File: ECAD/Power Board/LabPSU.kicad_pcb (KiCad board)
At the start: 2 copper layers, 82 parts, among them J1 CTRL, J2 DC-IN, J3 UPDI, J4 +, J5 -, Q1 Si7148DP, Q2 Si7148DP, U1 LM1117-3.3, U2 LM2594HVN-5.0, U3 LM5118MH, U4 TXB0104D, U5 LM358, U6 ATtiny414-SS, U7 INA180A3, U8 MCP4811

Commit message: route
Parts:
- C14, C16, C6, C8: footprint Capacitor_SMD:C_0805_2012Metric -> Capacitor_SMD:C_0603_1608Metric
- R7: footprint Resistor_SMD:R_0805_2012Metric -> Capacitor_SMD:C_0603_1608Metric
- moved TP6 35.7 mm to (69.3, 69.3)
- moved TP10 26.8 mm to (84.8, 95.2)
- moved C9 23.9 mm to (70.4, 86.9), turned to 0 degrees
- moved C11 23.9 mm to (94.2, 86.7), turned to 90 degrees
- moved TP8 19.9 mm to (112.8, 68.3)
- moved C23 2.97 mm to (127.8, 93.5)
- moved C25 2.74 mm to (127.8, 104.6)
- moved C20 2.59 mm to (120.7, 106.4)
- moved C19 2.59 mm to (118.1, 91.7)
- moved C22 2.59 mm to (118.1, 97.8)
- moved R4 2.34 mm to (90.9, 89.7)
- moved C12 2.30 mm to (103.9, 94.0)
- moved R3 2.16 mm to (88.6, 90.4)
- moved R1 1.70 mm to (85.3, 87.1)
- moved R2 1.70 mm to (85.3, 90.6)
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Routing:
- net VBUS: track 33.8 -> 74.0 mm
- net Net-(C15-Pad2): track 0.00 -> 31.1 mm
- net Net-(Q2-Pad4): track 0.00 -> 27.7 mm
- net EN: track 0.00 -> 17.5 mm
- net Net-(R1-Pad2): track 0.00 -> 12.6 mm, vias 0 -> 2
- net /FB: track 0.00 -> 7.09 mm
- net Net-(R3-Pad1): track 0.00 -> 6.84 mm
- net Net-(C6-Pad1): track 0.00 -> 6.17 mm
- net Net-(C14-Pad2): track 0.00 -> 5.56 mm
- net Net-(C8-Pad1): track 0.00 -> 3.82 mm
- net GND: track 14.1 -> 17.9 mm
- net Net-(C12-Pad1): track 0.00 -> 3.80 mm
- net Net-(C15-Pad1): track 0.00 -> 3.65 mm
- net VOUT: track 0.00 -> 2.96 mm
- net Net-(C14-Pad1): track 0.00 -> 1.50 mm

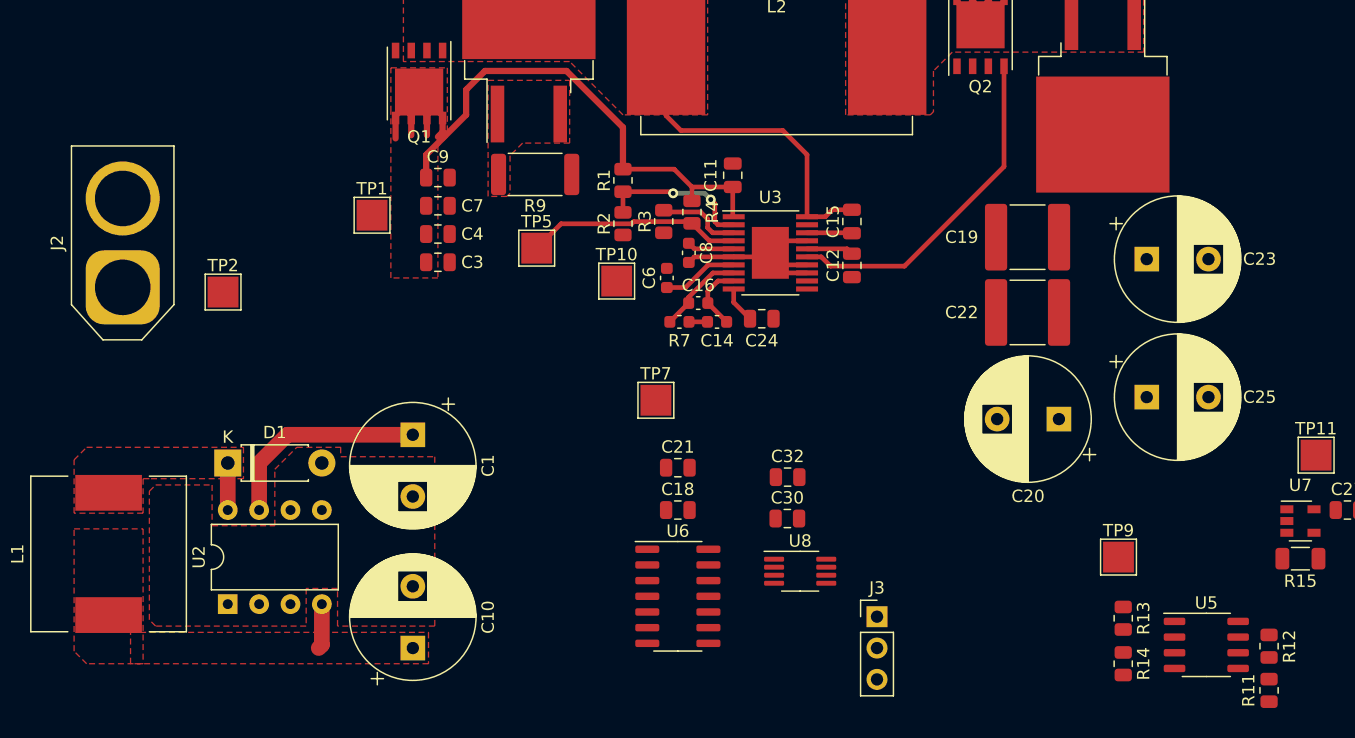
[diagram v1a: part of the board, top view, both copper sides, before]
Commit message: kelvin connection for shunt resistor
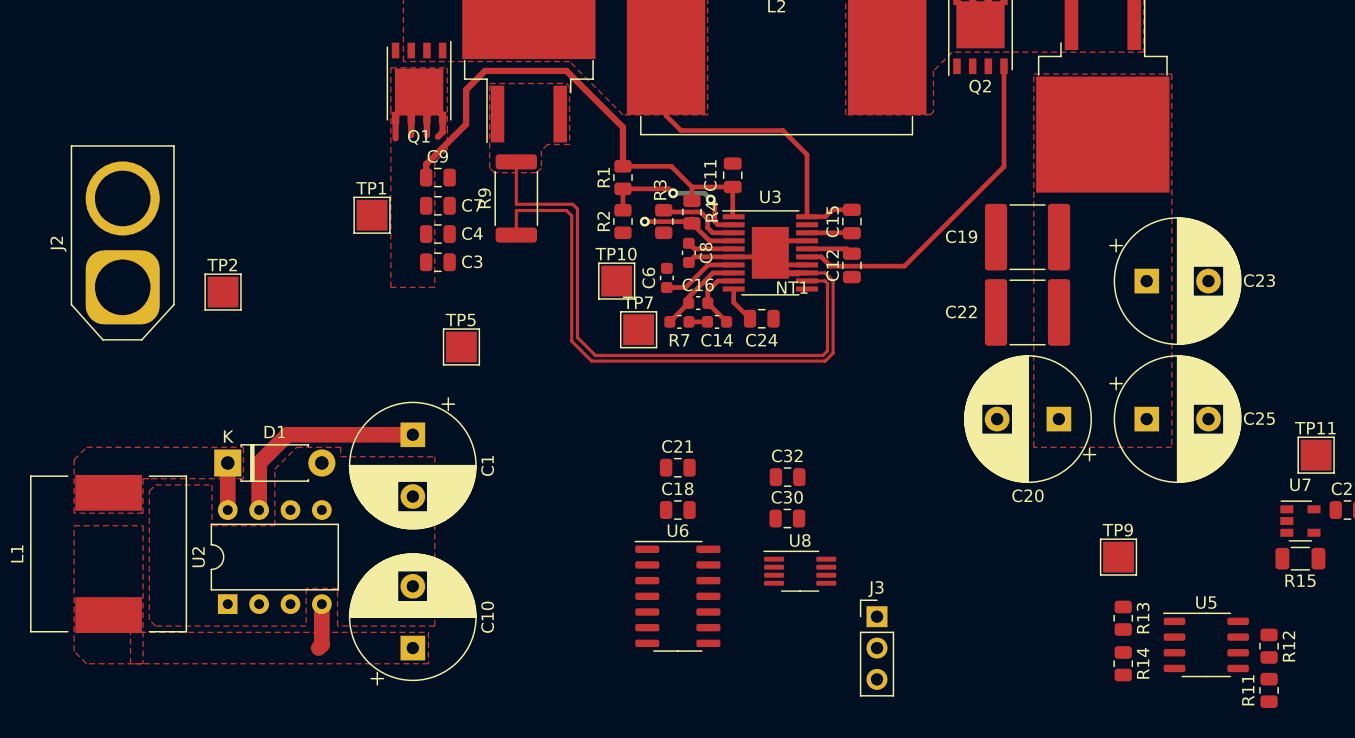
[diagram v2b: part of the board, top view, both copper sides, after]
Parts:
- added NT1: Kelvin Tie, NetTie:NetTie-2_SMD_Pad0.5mm, F.Cu at (99.1, 94.6)
- moved TP5 10.1 mm to (72.3, 100.6)
- moved TP7 5.88 mm to (86.6, 99.2)
- moved R9 2.47 mm to (76.7, 88.6), turned to 270 degrees
- moved C23 1.78 mm to (127.8, 95.2)
- moved C25 1.78 mm to (127.8, 106.4)
- moved R1 0.23 mm to (85.3, 86.9)
- moved R2 0.18 mm to (85.3, 90.4)
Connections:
- R9 pad 2: GND -> Net-(NT1-Pad1)
- U3 pad 13: GND -> Net-(NT1-Pad1)
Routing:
- net Net-(NT1-Pad1): track 0.00 -> 47.8 mm
- net Net-(D2-Pad2): track 0.00 -> 47.2 mm
- net EN: track 17.5 -> 7.84 mm, vias 0 -> 1
- net GND: track 17.9 -> 16.8 mm
- added copper zone on F.Cu, net Net-(C19-Pad1)
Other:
- board text added: "Matched Length Kelvin Pair"

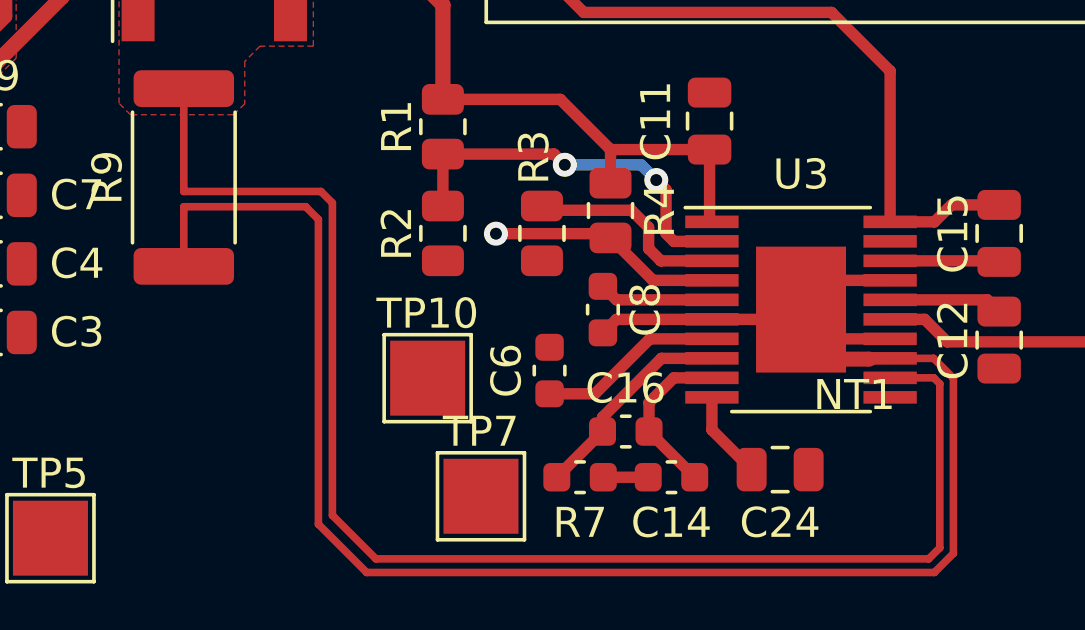
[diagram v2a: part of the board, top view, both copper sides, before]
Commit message: Correct net tie placement
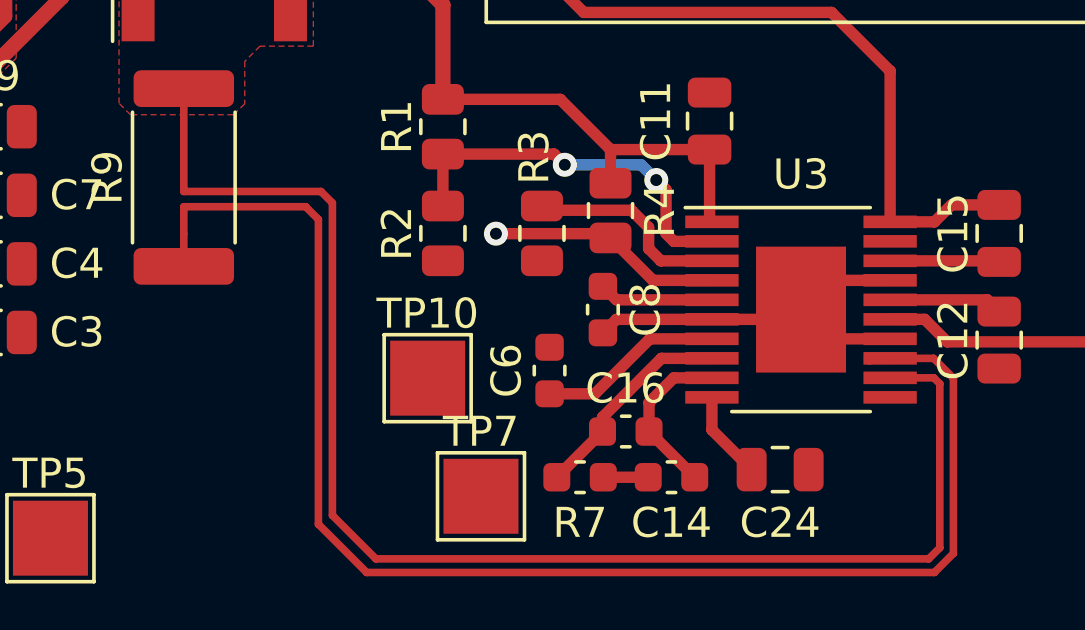
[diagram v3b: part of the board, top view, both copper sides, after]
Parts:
- moved NT1 22.7 mm to (76.7, 90.9), turned to 270 degrees
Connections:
- R9 pad 2: Net-(NT1-Pad1) -> GND
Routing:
- net GND: track 16.8 -> 15.0 mm
- net Net-(NT1-Pad1): track 47.8 -> 46.7 mm

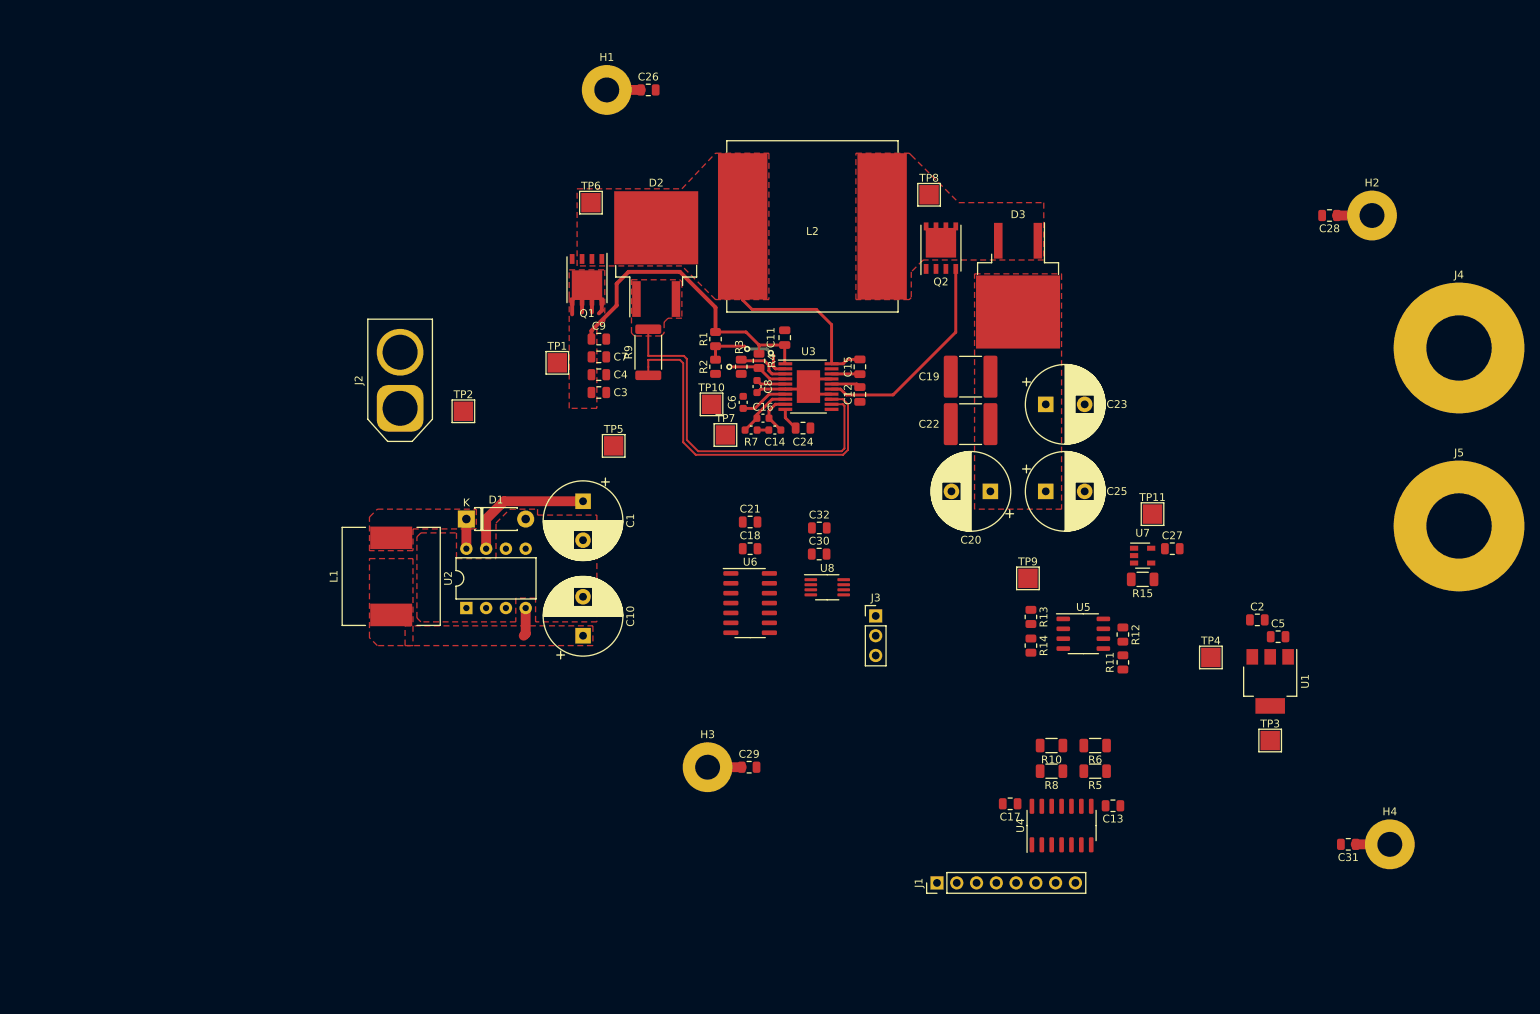
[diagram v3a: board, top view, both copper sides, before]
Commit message: Routing and mask removal
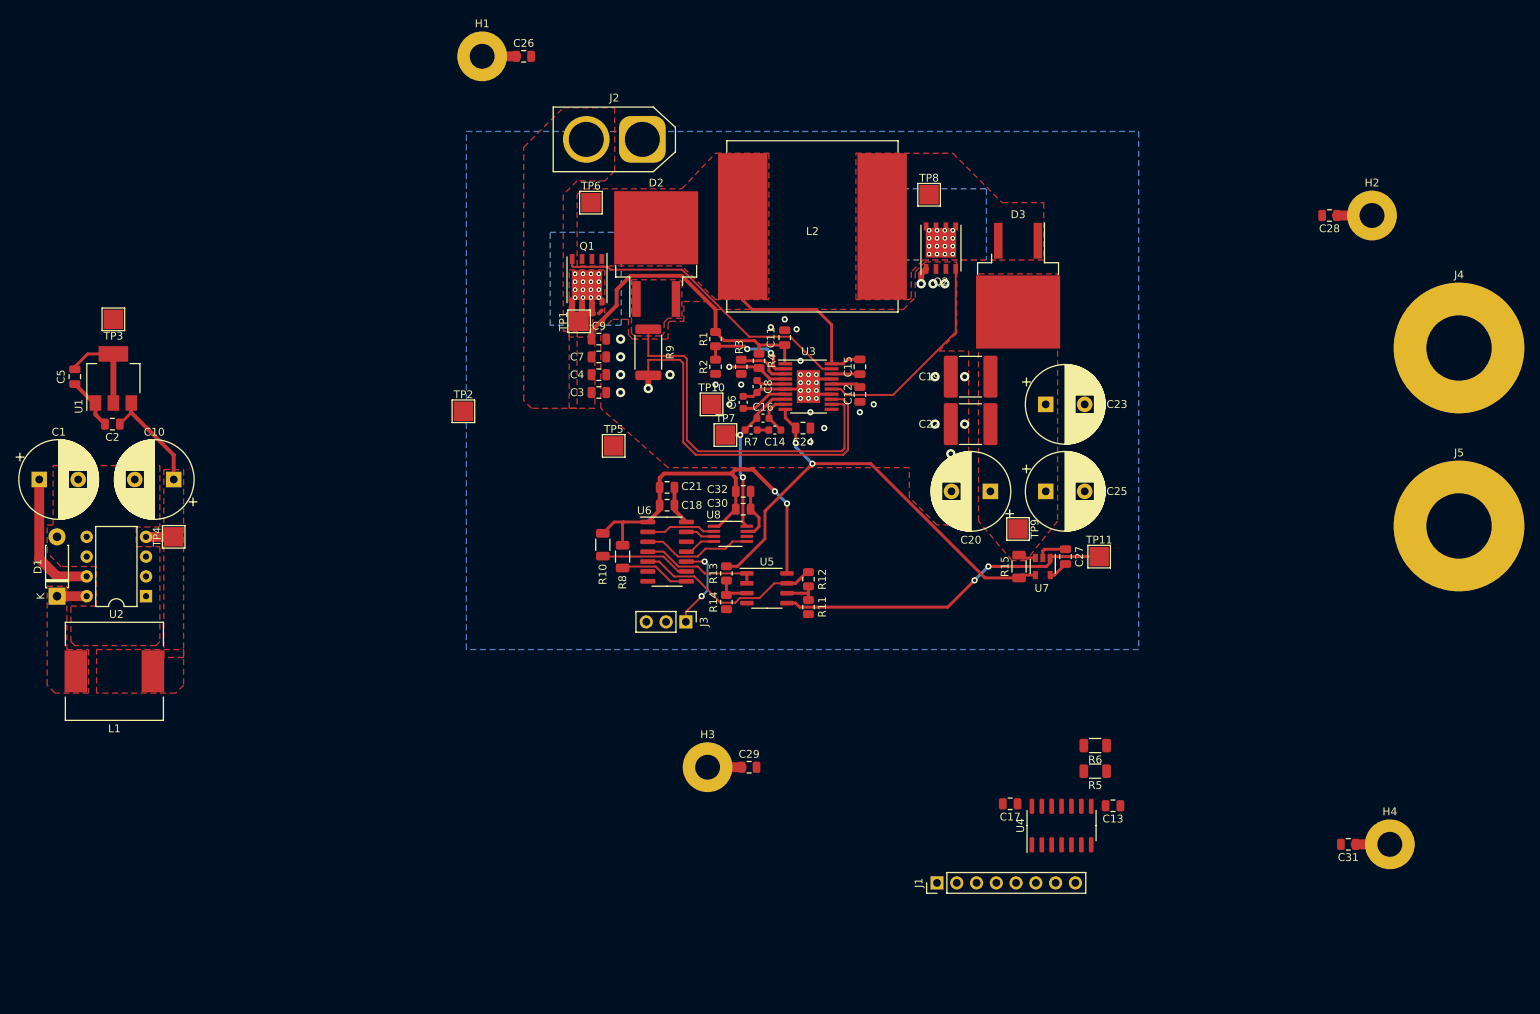
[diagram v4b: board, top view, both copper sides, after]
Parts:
- moved TP3 158.1 mm to (8.00, 84.3), turned to 180 degrees
- moved C5 158.1 mm to (3.05, 91.7), turned to 270 degrees
- moved U1 153.6 mm to (8.00, 91.9), turned to 90 degrees
- moved C2 149.2 mm to (7.87, 97.8), turned to 180 degrees
- moved TP4 134.1 mm to (15.7, 112.3), turned to 90 degrees
- moved C1 69.9 mm to (-1.52, 104.9), turned to 0 degrees
- moved R10 63.1 mm to (70.9, 113.3), turned to 270 degrees
- moved R8 61.6 mm to (73.4, 114.8), turned to 270 degrees
- moved C10 56.3 mm to (15.7, 104.9), turned to 180 degrees
- moved D1 53.5 mm to (0.76, 119.9), turned to 90 degrees
- moved J2 46.5 mm to (75.9, 61.2), turned to 180 degrees
- moved U2 41.2 mm to (12.2, 119.9), turned to 180 degrees
- moved U5 41.1 mm to (91.9, 118.9)
- moved R11 41.0 mm to (97.3, 121.3)
- moved R12 41.0 mm to (97.3, 117.7)
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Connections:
- J3 pad 2: +3V3 -> +5V
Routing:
- net +5V: track 3.66 -> 72.2 mm, vias 0 -> 2
- net VOUT: track 2.96 -> 61.9 mm, vias 0 -> 2
- net IOUT: track 0.00 -> 43.4 mm, vias 0 -> 2
- net Net-(Q1-Pad4): track 0.00 -> 39.7 mm
- net GND: track 15.0 -> 43.6 mm, vias 0 -> 38
- net IOUTBUF: track 0.00 -> 24.5 mm
- net VOUTBUF: track 0.00 -> 15.2 mm
- net /FB: track 7.09 -> 22.0 mm, vias 0 -> 2
- net /LDAC: track 0.00 -> 14.3 mm
- net +3V3: track 0.00 -> 12.3 mm
- net SCL: track 0.00 -> 11.5 mm
- net /UPDI: track 0.00 -> 11.4 mm, vias 0 -> 2
- net SDA: track 0.00 -> 9.05 mm
- net /CS0: track 0.00 -> 8.99 mm
- net VBUS: track 73.8 -> 66.1 mm, vias 0 -> 16
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- added copper zone on B.Cu, net GND
- added copper zone on B.Cu, net Net-(D3-Pad2)
- added copper zone on B.Cu, net VBUS

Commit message: route
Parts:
- moved L1 64.7 mm to (72.6, 134.7)
- moved D1 64.7 mm to (65.3, 125.1)
- moved C1 64.7 mm to (63.0, 110.1)
- moved C10 64.7 mm to (80.3, 110.1)
- moved TP4 64.7 mm to (80.3, 117.5)
- moved U2 64.7 mm to (76.7, 125.1)
- moved TP3 63.3 mm to (50.8, 130.9)
- moved U1 63.3 mm to (50.8, 138.5)
- moved C2 63.3 mm to (50.7, 144.4)
- moved C5 63.3 mm to (45.8, 138.3)
- moved TP2 45.9 mm to (82.8, 61.2)
- moved C18 14.5 mm to (93.6, 109.1)
- moved C21 14.5 mm to (93.6, 106.8)
- moved R11 14.5 mm to (111.8, 122.2)
- moved R12 14.5 mm to (111.8, 118.6)
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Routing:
- net IOUT: track 43.4 -> 29.2 mm
- net /FB: track 22.0 -> 35.9 mm, vias 2 -> 4
- net +5V: track 72.2 -> 61.4 mm, vias 2 -> 0
- net VOUT: track 61.9 -> 57.6 mm, vias 2 -> 4
